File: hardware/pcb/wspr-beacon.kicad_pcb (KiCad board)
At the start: 2 copper layers, 100 x 100 mm, 73 parts, among them J1 USB_OTG, J2 Conn_01x04, J3 Conn_02x03_Odd_Even, J4 Conn_Coaxial, J5 Conn_Coaxial, J6 Conn_Coaxial, SW1 SW_Push, U1 AP1117-33, U2 ATMEGA328-AU, U3 Si5351A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

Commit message: First finished version of layout
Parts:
- added C24: 100n, Capacitors_SMD:C_0805_HandSoldering, F.Cu at (65.6, 99.1)
- added D5: LED, LEDs:LED_0805_HandSoldering, F.Cu at (75.6, 65.6)
- added R14: R, Resistors_SMD:R_0805_HandSoldering, F.Cu at (75.6, 69.1)
- moved R8 47.9 mm to (75.6, 76.1), turned to 180 degrees
- moved J3 46.4 mm to (75.1, 110.1), turned to 90 degrees
- moved SW1 46.2 mm to (90.1, 115.1)
- moved D1 45.2 mm to (75.6, 72.6), turned to 180 degrees
- moved R6 38.5 mm to (62.1, 90.1), turned to 180 degrees
- moved J2 37.9 mm to (53.1, 88.1)
- moved R7 37.5 mm to (62.1, 93.6), turned to 180 degrees
- moved U2 35.5 mm to (75.6, 96.6)
- moved C4 31.5 mm to (88.4, 99.9), turned to 270 degrees
- moved X2 31.0 mm to (66.6, 104.6)
- moved C11 29.6 mm to (61.6, 104.8), turned to 270 degrees
- moved C3 28.5 mm to (84.8, 99.9), turned to 270 degrees
- moved R2 28.0 mm to (63.1, 65.6), turned to 180 degrees
- moved J1 27.9 mm to (51.6, 71.1)
- moved R4 27.5 mm to (63.1, 69.1)
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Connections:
- R2 pad 1: Net-(J1-Pad2) -> +3V3
- R2 pad 2: +3V3 -> Net-(J1-Pad2)
- R6 pad 1: Net-(J2-Pad2) -> Net-(R6-Pad1)
- R6 pad 2: Net-(R6-Pad2) -> Net-(J2-Pad2)
- R7 pad 1: Net-(J2-Pad3) -> Net-(R7-Pad1)
- R7 pad 2: Net-(R7-Pad2) -> Net-(J2-Pad3)
- U2 pad 23: /LED_CLK0 -> /LED_CLK2
- U2 pad 25: /LED_CLK2 -> /LED_CLK0
- U2 pad 30: Net-(R6-Pad2) -> Net-(R6-Pad1)
- U2 pad 31: Net-(R7-Pad2) -> Net-(R7-Pad1)
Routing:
- net +3V3: track 108.0 -> 213.5 mm, vias 0 -> 4
- net Net-(R6-Pad2): track 37.8 -> 0.00 mm, vias 2 -> 0
- net Net-(R7-Pad2): track 34.8 -> 0.00 mm, vias 2 -> 0
- net VBUS: track 56.7 -> 22.2 mm
- net /LED_CLK2: track 47.3 -> 72.4 mm, vias 2 -> 0
- net /LED_CLK0: track 89.4 -> 69.1 mm
- net /MOSI: track 44.5 -> 24.5 mm, vias 0 -> 2
- net GND: track 137.1 -> 156.1 mm, vias 41 -> 44
- net Net-(R6-Pad1): track 0.00 -> 18.1 mm, vias 0 -> 2
- net Net-(C14-Pad1): track 34.6 -> 51.7 mm
- net /MISO: track 27.7 -> 10.6 mm
- net Net-(C12-Pad1): track 36.1 -> 19.7 mm
- net /LED_CLK1: track 73.3 -> 56.9 mm
- net Net-(R7-Pad1): track 0.00 -> 15.7 mm, vias 0 -> 2
- net Net-(C13-Pad1): track 17.3 -> 32.5 mm
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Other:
- board size 100 x 100 mm -> 100 x 70 mm
- rule trace_min: 0.2 -> 0.25
- board text added: "3V3 MOSI GND"
- board text added: "3V3 RX TX GND"
- board text added: "MISO SCK RST"

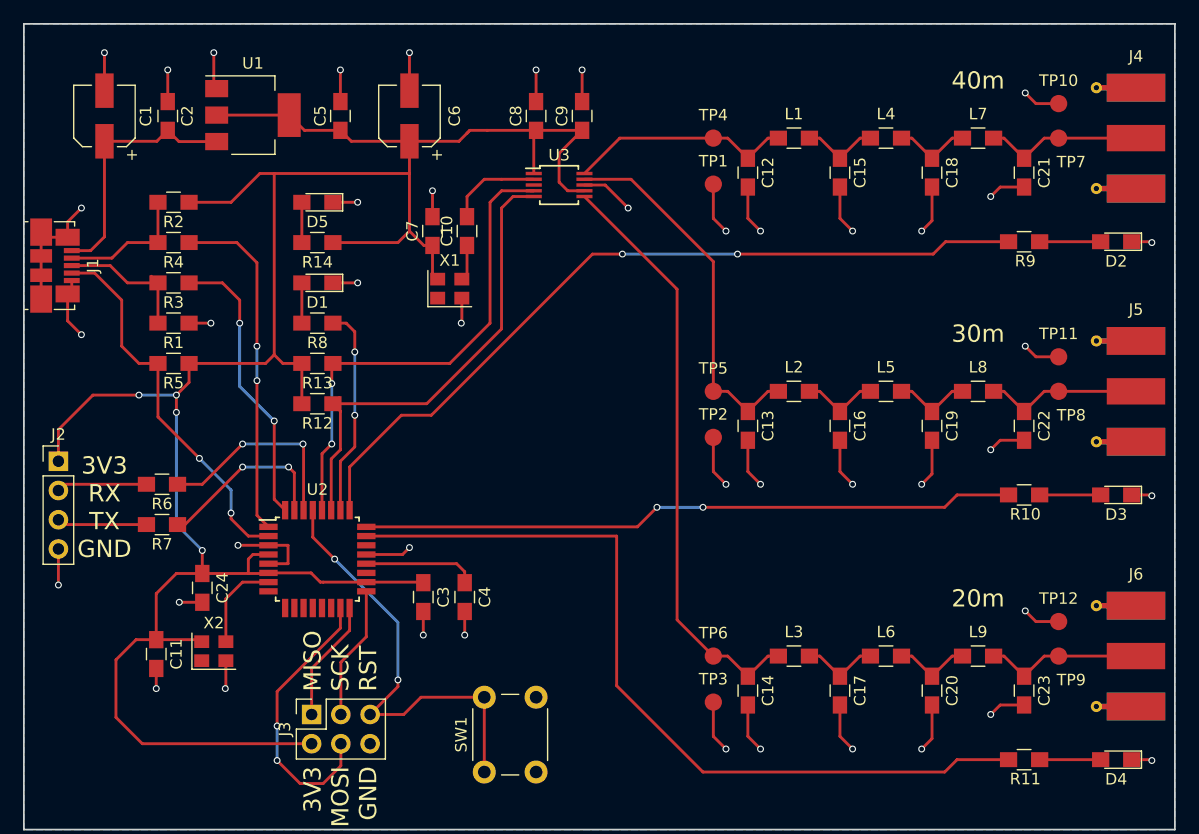
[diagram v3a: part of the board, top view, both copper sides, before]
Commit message: Increase via size
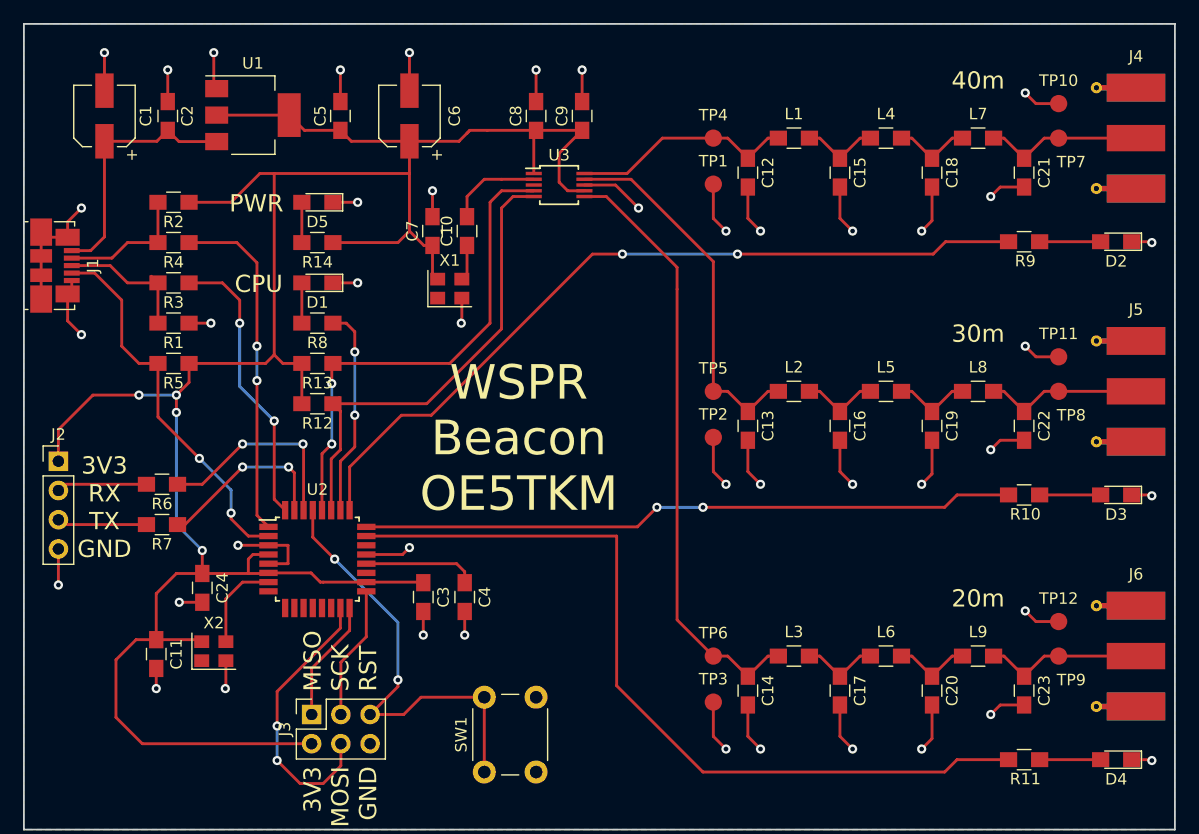
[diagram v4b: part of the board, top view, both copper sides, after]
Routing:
- net Net-(C14-Pad1): track 51.7 -> 52.8 mm
- net GND: track 156.1 -> 157.0 mm
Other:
- net class Default: via_dia 0.6 -> 0.8
- rule via_min_drill: 0.3 -> 0.4
- rule via_min_size: 0.4 -> 0.8
- board text added: "CPU"
- board text added: "PWR"
- board text added: "WSPR Beacon OE5TKM"

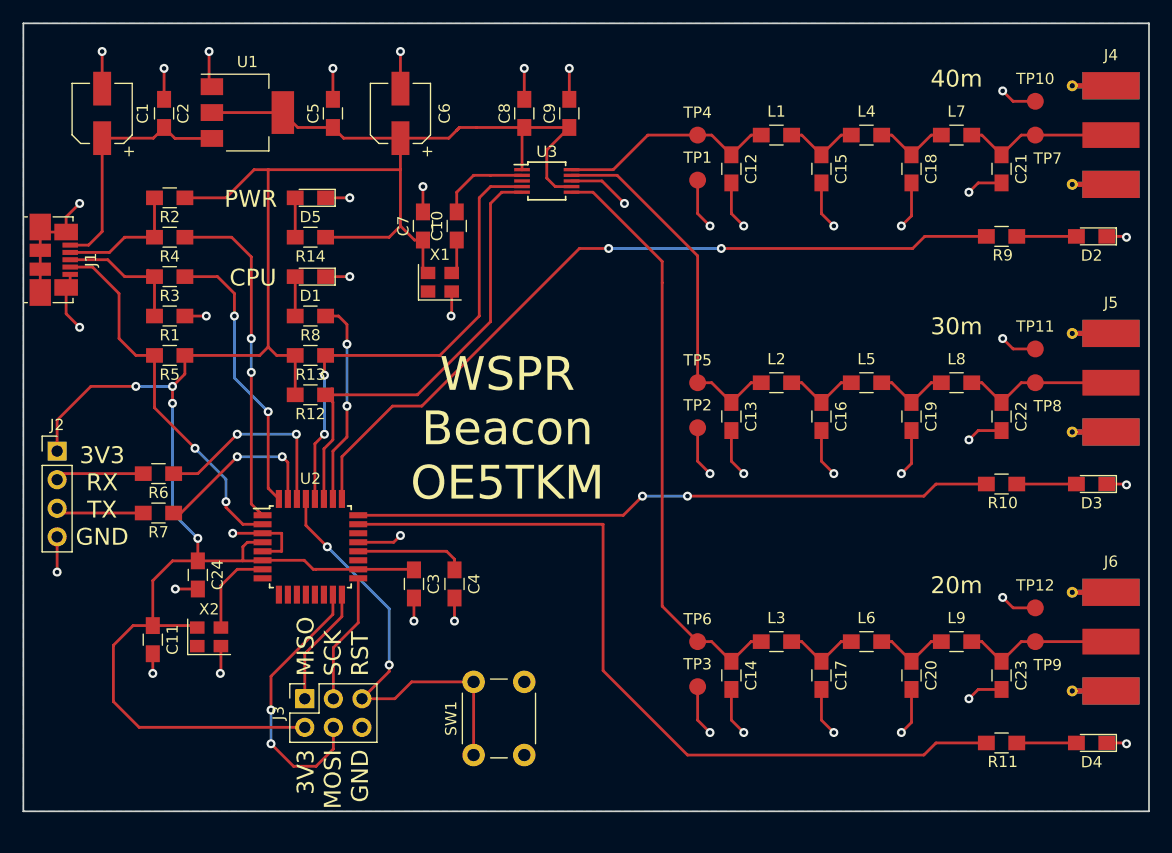
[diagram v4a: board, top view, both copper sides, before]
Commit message: Update to KiCad 5
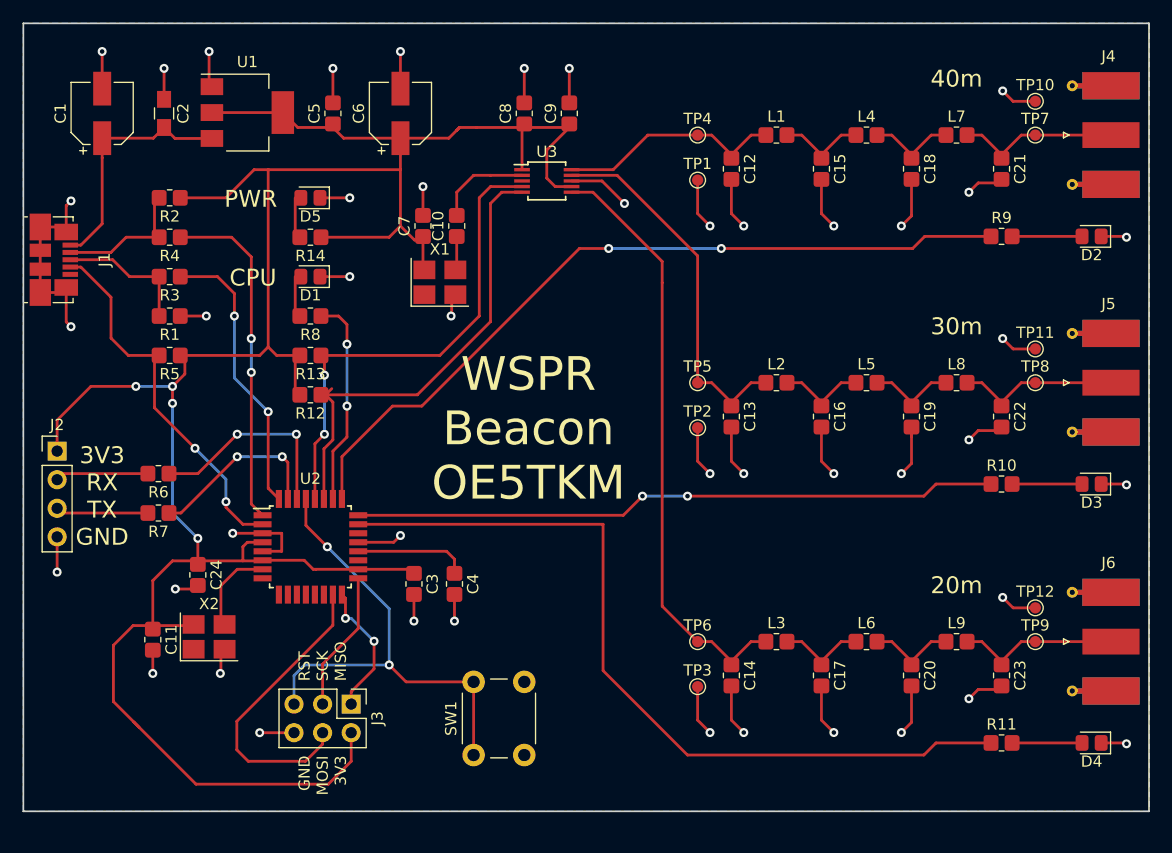
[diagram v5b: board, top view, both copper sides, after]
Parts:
- C1, C6: footprint Capacitors_SMD:CP_Elec_5x5.7 -> Capacitor_SMD:CP_Elec_5x5.4
- C10, C11, C12, C13, C14, C15, C16, C17, C18, C19, C20, C21, C22, C23, C24, C3, C4, C5, C7, C8, C9: footprint Capacitors_SMD:C_0805_HandSoldering -> Capacitor_SMD:C_0805_2012Metric_Pad1.33x1.40mm_HandSolder
- D1, D2, D3, D4, D5: footprint LEDs:LED_0805_HandSoldering -> LED_SMD:LED_0805_2012Metric_Pad1.15x1.40mm_HandSolder
- J1: footprint Connectors_USB:USB_Micro-B_Molex_47346-0001 -> Connector_USB:USB_Micro-B_Molex_47346-0001
- J2: footprint Pin_Headers:Pin_Header_Straight_1x04_Pitch2.54mm -> Connector_PinHeader_2.54mm:PinHeader_1x04_P2.54mm_Vertical
- J3: footprint Socket_Strips:Socket_Strip_Straight_2x03_Pitch2.54mm -> Connector_PinHeader_2.54mm:PinHeader_2x03_P2.54mm_Vertical
- J4, J5, J6: footprint Connectors_Molex:Molex_SMA_Jack_Edge_Mount -> Connector_Coaxial:SMA_Molex_73251-1153_EdgeMount_Horizontal
- L1, L2, L3, L4, L5, L6, L7, L8, L9: footprint Inductors_SMD:L_0805_HandSoldering -> Inductor_SMD:L_0805_2012Metric_Pad1.33x1.40mm_HandSolder
- R1, R10, R11, R12, R13, R14, R2, R3, R4, R5, R6, R7, R8, R9: footprint Resistors_SMD:R_0805_HandSoldering -> Resistor_SMD:R_0805_2012Metric_Pad1.33x1.40mm_HandSolder
- SW1: footprint Buttons_Switches_THT:SW_PUSH_6mm -> Button_Switch_THT:SW_PUSH_6mm
- TP1, TP10, TP11, TP12, TP2, TP3, TP4, TP5, TP6, TP7, TP8, TP9: footprint Measurement_Points:Measurement_Point_Round-SMD-Pad_Small -> TestPoint:TestPoint_Pad_D1.0mm
- U1: footprint TO_SOT_Packages_SMD:SOT-223-3_TabPin2 -> Package_TO_SOT_SMD:SOT-223-3_TabPin2
- U2: footprint Housings_QFP:TQFP-32_7x7mm_Pitch0.8mm -> Package_QFP:TQFP-32_7x7mm_P0.8mm
- U3: footprint Housings_SSOP:MSOP-10_3x3mm_Pitch0.5mm -> Package_SO:MSOP-10_3x3mm_P0.5mm
- X1, X2: footprint Oscillators:Oscillator_SMD_Abracon_ASE-4pin_3.2x2.5mm -> Oscillator:Oscillator_SMD_Abracon_ASE-4Pin_3.2x2.5mm_HandSoldering
- moved J3 4.15 mm to (79.2, 110.6), turned to 270 degrees
- moved J1 1.21 mm to (52.8, 71.1)
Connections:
- J4 pad 1: Net-(C21-Pad1) -> Net-(J4-Pad1)
- J5 pad 1: Net-(C22-Pad1) -> Net-(J5-Pad1)
- J6 pad 1: Net-(C23-Pad1) -> Net-(J6-Pad1)
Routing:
- net +3V3: track 213.5 -> 223.7 mm
- net /RESET: track 39.0 -> 43.9 mm
- net GND: track 157.0 -> 161.4 mm, vias 44 -> 45
- net /MOSI: track 24.5 -> 27.0 mm, vias 2 -> 0
- net /MISO: track 10.6 -> 12.0 mm, vias 0 -> 2
- net /SCK: track 11.6 -> 12.5 mm
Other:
- board text added: "GND MOSI 3V3"
- board text added: "RST SCK MISO"
- board text removed: "3V3 MOSI GND"
- board text removed: "MISO SCK RST"

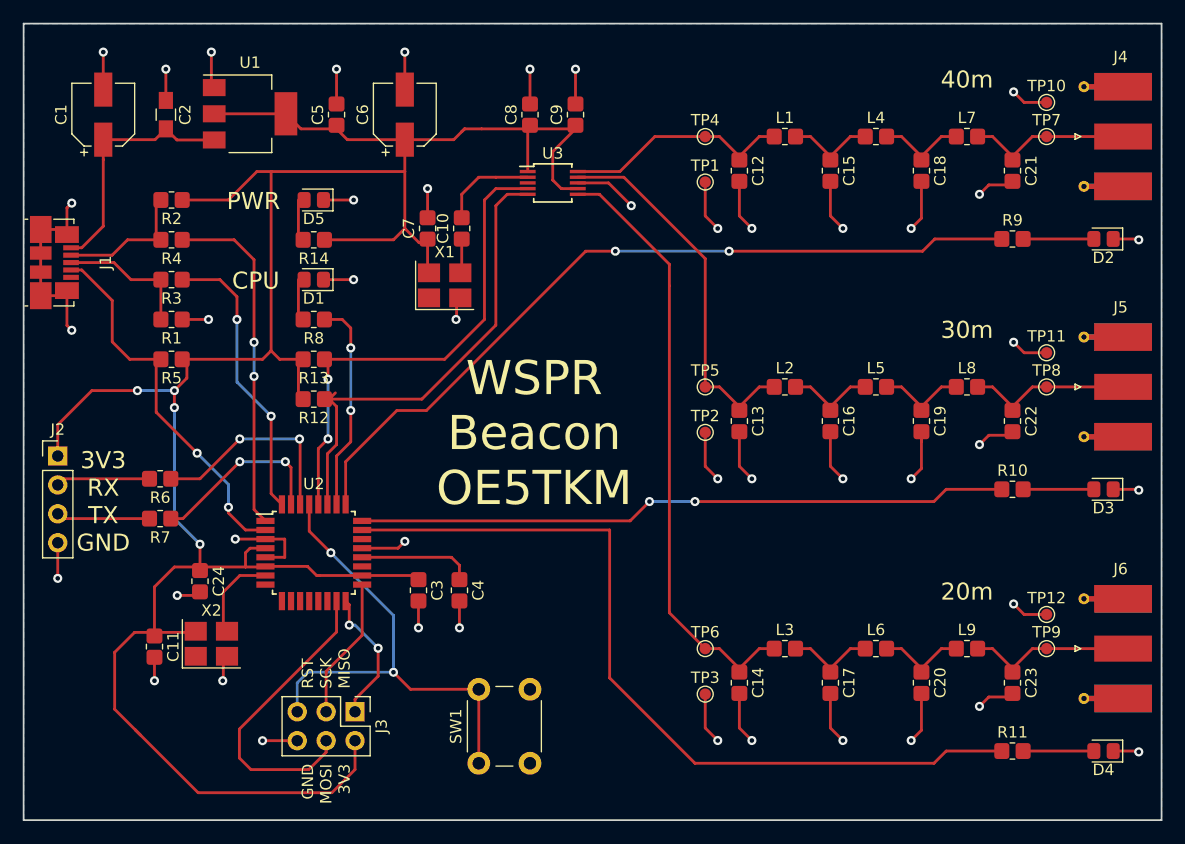
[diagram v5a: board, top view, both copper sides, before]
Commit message: Place 20m output closer to Si5351
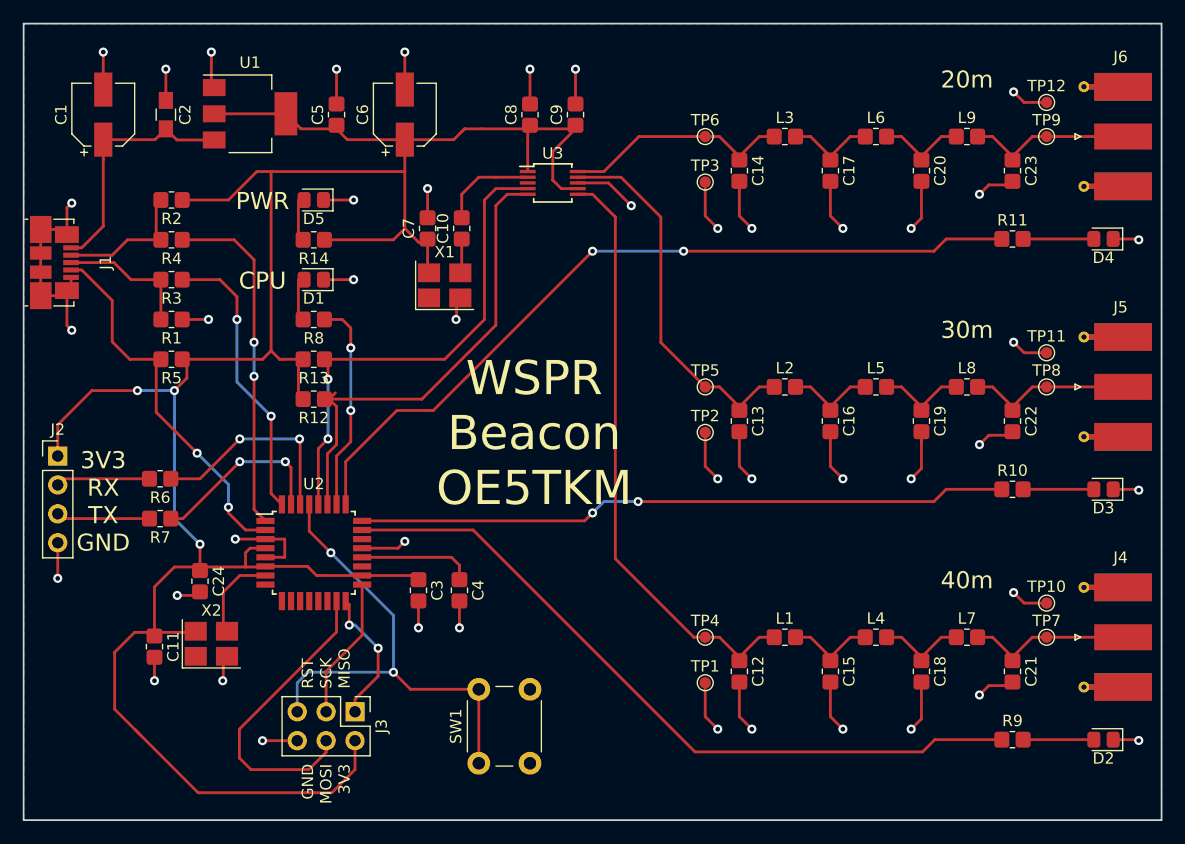
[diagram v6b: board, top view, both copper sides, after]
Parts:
- moved C14 45.0 mm to (113.0, 63.0)
- moved C17 45.0 mm to (121.0, 63.0)
- moved C20 45.0 mm to (129.0, 63.0)
- moved C23 45.0 mm to (137.0, 63.0)
- moved D4 45.0 mm to (145.0, 69.0)
- moved J6 45.0 mm to (145.0, 60.0)
- moved L3 45.0 mm to (117.0, 60.0)
- moved L6 45.0 mm to (125.0, 60.0)
- moved L9 45.0 mm to (133.0, 60.0)
- moved R11 45.0 mm to (137.0, 69.0)
- moved TP12 45.0 mm to (140.0, 57.0)
- moved TP3 45.0 mm to (110.0, 64.0)
- moved TP6 45.0 mm to (110.0, 60.0)
- moved TP9 45.0 mm to (140.0, 60.0)
- moved C12 44.0 mm to (113.0, 107.0)
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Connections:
- net /LED_CLK1 renamed /LED_30M
- J4 pad 1: Net-(J4-Pad1) -> Net-(C21-Pad1)
- J5 pad 1: Net-(J5-Pad1) -> Net-(C22-Pad1)
- J6 pad 1: Net-(J6-Pad1) -> Net-(C23-Pad1)
- R11 pad 1: /LED_CLK2 -> /LED_40M
- R9 pad 1: /LED_CLK0 -> /LED_20M
- U2 pad 23: /LED_CLK2 -> /LED_20M
- U2 pad 25: /LED_CLK0 -> /LED_40M
- U3 pad 10: Net-(C12-Pad1) -> Net-(C14-Pad1)
- U3 pad 6: Net-(C14-Pad1) -> Net-(C12-Pad1)
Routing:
- net /LED_CLK2: track 72.4 -> 0.00 mm
- net /LED_CLK0: track 69.1 -> 0.00 mm, vias 2 -> 0
- net /LED_40M: track 0.00 -> 69.1 mm, vias 0 -> 2
- net /LED_20M: track 0.00 -> 64.3 mm
- net Net-(C14-Pad1): track 52.8 -> 19.6 mm
- net Net-(C12-Pad1): track 19.7 -> 52.1 mm
- net GND: track 161.4 -> 182.9 mm
- net +3V3: vias 4 -> 3
